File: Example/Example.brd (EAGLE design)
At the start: 86 x 54 mm, 27 parts, among them IC2 74LS02D, U1 CD4017

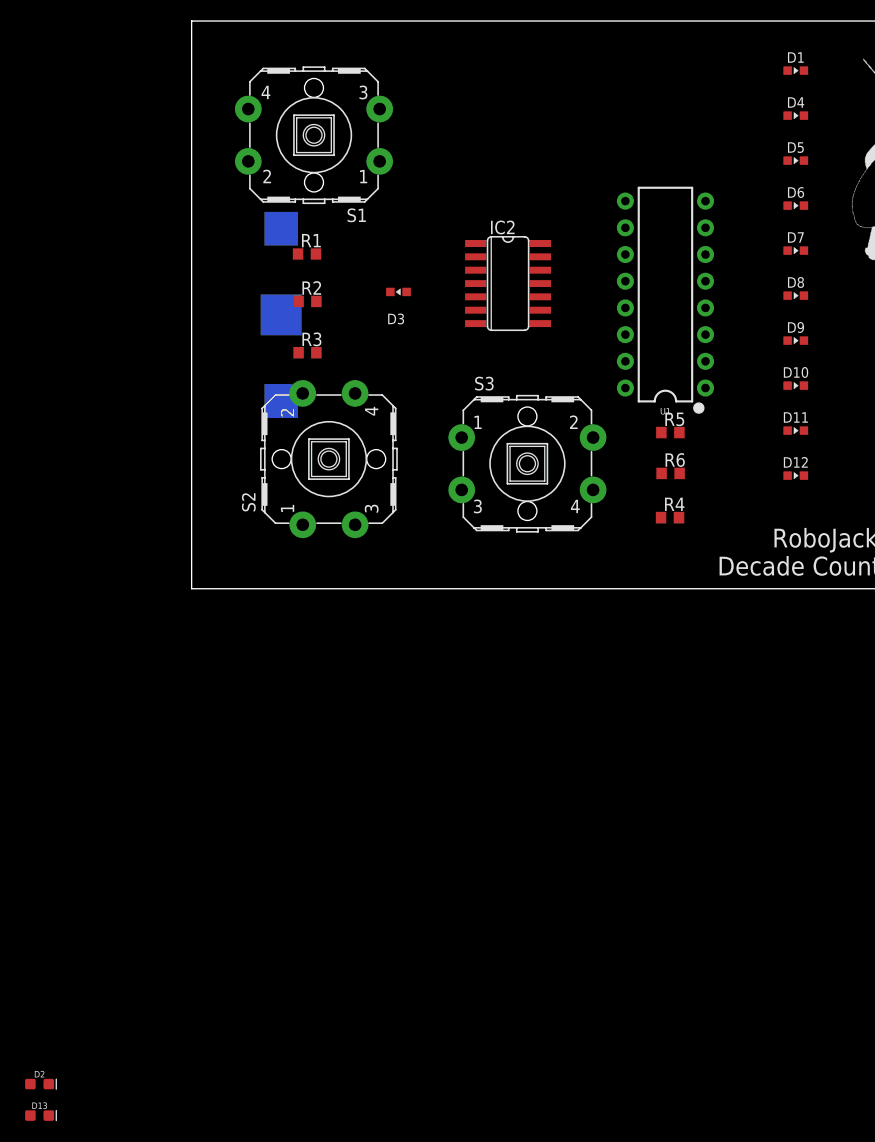
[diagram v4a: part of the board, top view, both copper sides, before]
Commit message: connected the reset button and change the titles for sheet
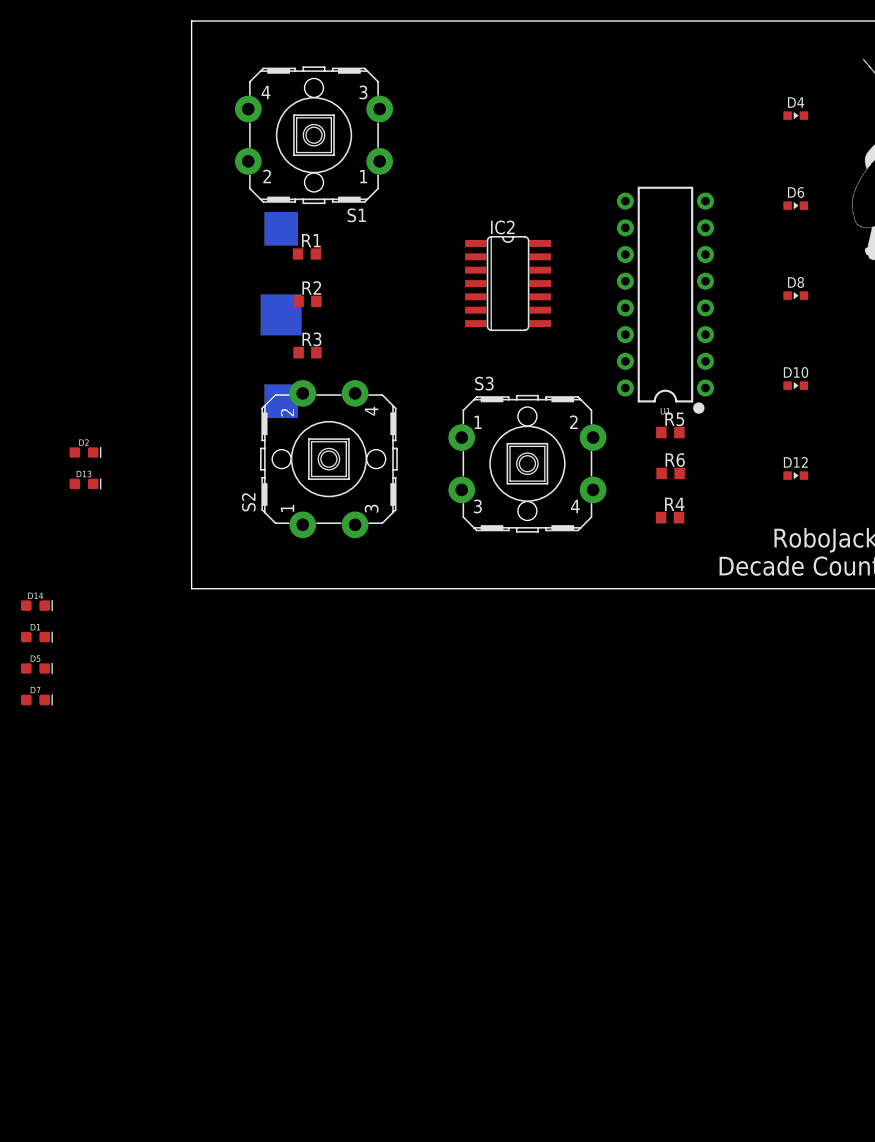
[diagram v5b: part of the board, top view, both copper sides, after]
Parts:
- removed D11, D3, D9: YELLOW, RoboJackets-LEDs:LED0603
- added D14: BLUE, RoboJackets-LEDs:LED-0603
- D1, D5, D7: value YELLOW -> BLUE; device RoboJackets-LEDs:LED0603 -> RoboJackets-LEDs:LED-0603
- moved D1 90.2 mm to (-14.8, -4.60)
- moved D5 87.0 mm to (-14.8, -7.59)
- moved D7 84.0 mm to (-14.8, -10.6)
- moved D13 60.2 mm to (-10.2, 9.97)
- moved D2 60.2 mm to (-10.2, 13.0)
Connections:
- removed net N$21: R5.2, U1.15
- new net N$1: S3.3
- new net N$3: R5.2, S3.1, U1.15
- net N$10: now also D2.A; no longer D1.A
- net N$12: now also D1.A; no longer D5.A
- net N$14: now also D5.A; no longer D7.A
- net N$16: now also D7.A; no longer D9.A
- net N$18: now also D14.A; no longer D11.A
- net N$2: now also D13.A; no longer D3.A
- net N$20: now also D14.C, D2.C; no longer D11.C, D9.C
- net N$5: now also D13.C; no longer D3.C
- net VCC: now also U1.16

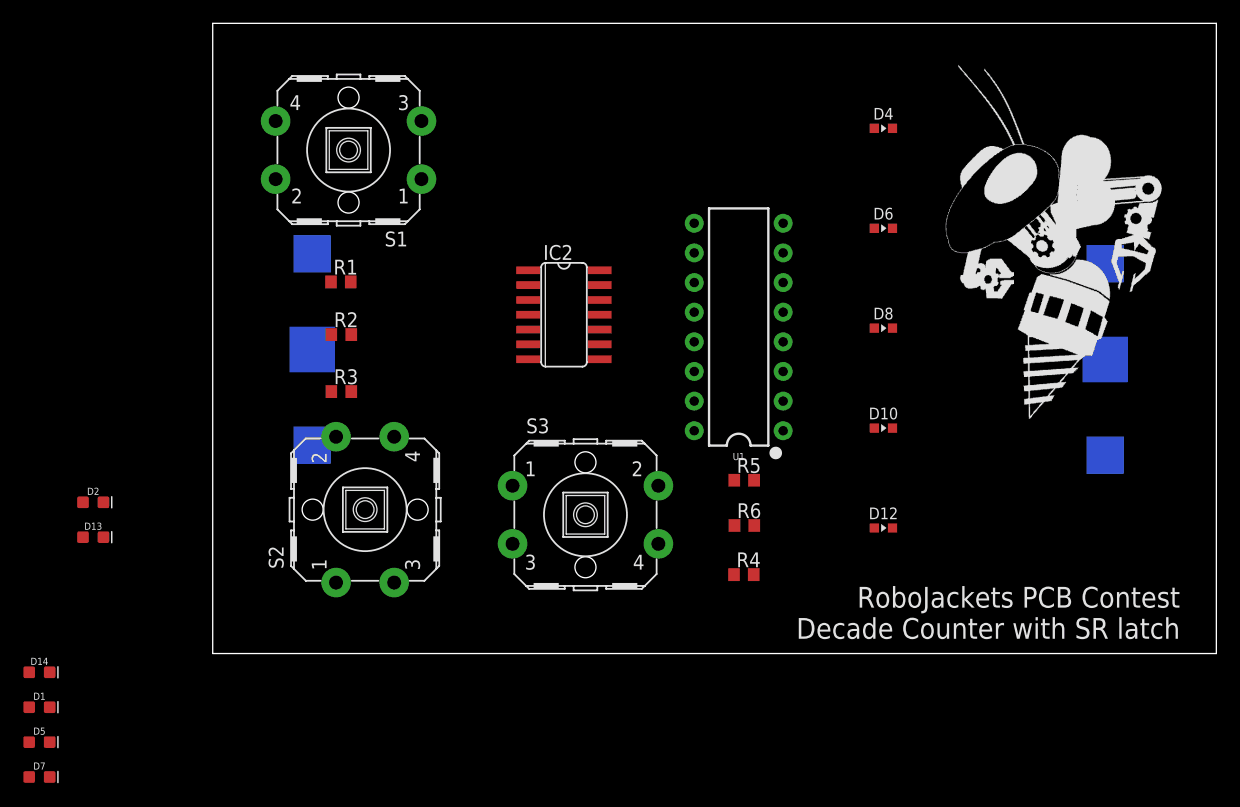
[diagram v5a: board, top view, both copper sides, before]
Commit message: change button and led position
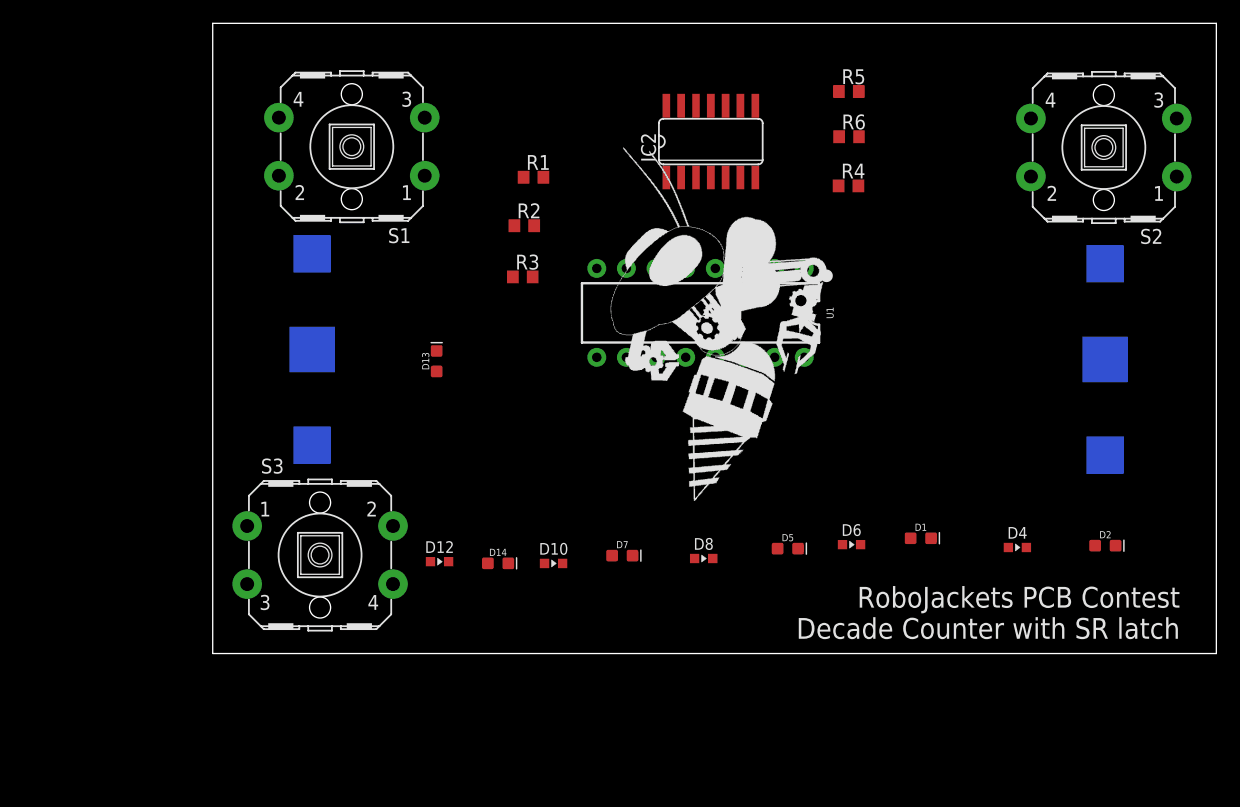
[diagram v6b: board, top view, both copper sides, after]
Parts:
- moved D2 86.8 mm to (76.5, 9.24)
- moved D1 76.9 mm to (60.7, 9.88)
- moved S2 70.5 mm to (76.4, 43.4), turned to 180 degrees
- moved D5 66.2 mm to (49.3, 8.99)
- moved D7 53.4 mm to (35.1, 8.39)
- moved D14 40.4 mm to (24.4, 7.73)
- moved D12 38.1 mm to (19.4, 7.87)
- moved D4 37.7 mm to (69.0, 9.09)
- moved R4 34.5 mm to (54.5, 40.1)
- moved R6 34.5 mm to (54.5, 44.3)
- moved R5 34.5 mm to (54.5, 48.2)
- moved D13 33.1 mm to (19.2, 25.1), turned to 90 degrees
- moved D10 30.5 mm to (29.2, 7.72)
- moved U$2 29.6 mm to (41.2, 13.1)
- moved D6 27.2 mm to (54.7, 9.33)
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
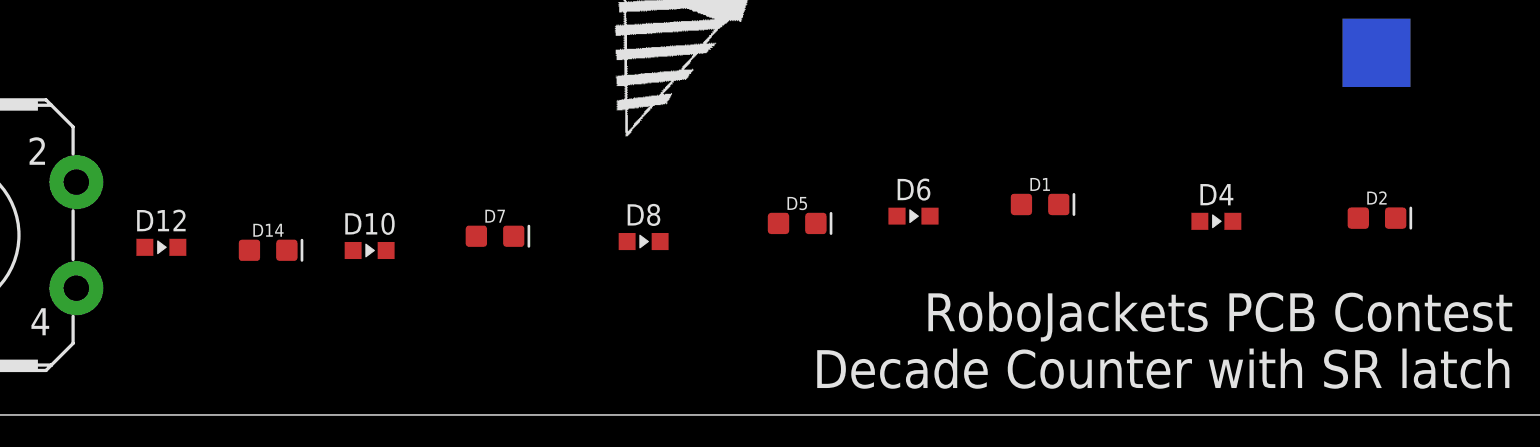
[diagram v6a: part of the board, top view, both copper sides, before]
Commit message: aligned LEDs
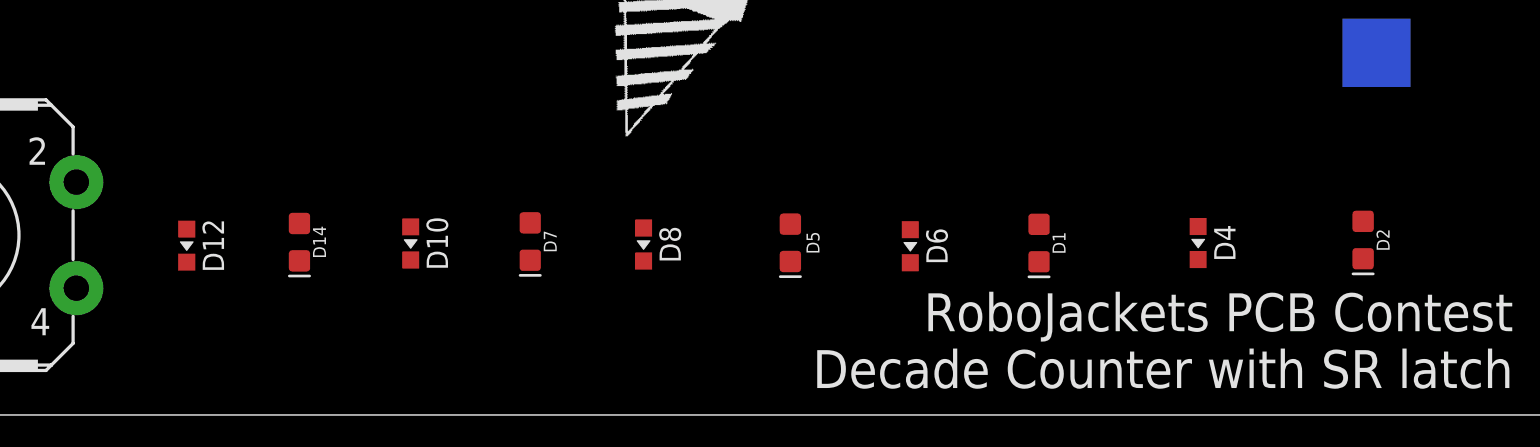
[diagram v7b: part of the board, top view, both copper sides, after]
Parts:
- moved D10 1.96 mm to (31.1, 8.05), turned to 270 degrees
- moved D1 1.81 mm to (60.6, 8.07), turned to 270 degrees
- moved D7 1.67 mm to (36.8, 8.14), turned to 270 degrees
- moved D14 1.52 mm to (25.9, 8.11), turned to 270 degrees
- moved D6 1.42 mm to (54.6, 7.92), turned to 270 degrees
- moved D4 1.33 mm to (68.1, 8.07), turned to 270 degrees
- moved D2 1.22 mm to (75.8, 8.21), turned to 270 degrees
- moved D12 1.19 mm to (20.6, 7.95), turned to 270 degrees
- moved D5 0.96 mm to (49.0, 8.08), turned to 270 degrees
- moved D8 0.14 mm to (42.1, 8.00), turned to 270 degrees

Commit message: moved parts
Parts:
- moved R4 23.6 mm to (61.2, 17.5)
- moved R6 21.9 mm to (61.2, 23.4)
- moved R5 20.6 mm to (61.4, 28.7)
- moved R3 15.0 mm to (26.9, 17.3)
- moved R2 14.0 mm to (27.0, 22.6)
- moved R1 12.5 mm to (27.0, 28.3)
- moved IC2 7.93 mm to (44.6, 36.2)
- moved U1 6.70 mm to (43.9, 22.8)
